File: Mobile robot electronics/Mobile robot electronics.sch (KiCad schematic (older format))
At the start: 17 parts

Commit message: added to schematic:
motor connectors, connections for the motor drivers, started the headers for the ultrasonics
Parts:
- added J? (x4): Conn_01x04_Male, symbol Connector:Conn_01x04_Male
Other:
- note added: "ESP32 MCU\n"
- note added: "Motor Connectors"
- note added: "Motor Drivers\n"

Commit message: added a correct part for ESP32 devkitc v4 wrover
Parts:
- removed U?: ESP32-DEVKITC-32D, MODULE_ESP32-DEVKITC-32D, symbol ESP32-DEVKITC-32D:ESP32-DEVKITC-32D
- added U?: ESP32-DevKitc-V4-WROVER, symbol MCU_ESP:ESP32-DevKitc-V4-WROVER
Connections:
- net labels added: MotorBLA, MotorBLB, MotorBRA, MotorBRB, MotorFLA, MotorFLB, MotorFRA, MotorFRB, Motor_BL_DIR, Motor_BL_PWM, Motor_BR_DIR, Motor_BR_PWM, Motor_FL_DIR, Motor_FL_PWM, Motor_FR_DIR, Motor_FR_PWM
- net labels removed: Motor1A, Motor1B, Motor2A, Motor2B, Motor3A, Motor3B, Motor4A, Motor4B, Motor_1_DIR, Motor_1_PWM, Motor_2_DIR, Motor_2_PWM, Motor_3_DIR, Motor_3_PWM, Motor_4_DIR, Motor_4_PWM
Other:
- note added: "motor BL"
- note added: "motor BR"
- note added: "motor FL"
- note added: "motor FR\n"
- note removed: "motor 1"
- note removed: "motor 2\n"
- note removed: "motor 3"
- note removed: "motor 4"
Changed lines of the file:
@@
 L power:GND #PWR?
 U 1 1 6073A39F
-P 2650 1200
-F 0 "#PWR?" H 2650 950 50  0001 C CNN
-F 1 "GND" V 2655 1072 50  0000 R CNN
-F 2 "" H 2650 1200 50  0001 C CNN
-F 3 "" H 2650 1200 50  0001 C CNN
-	1    2650 1200
+P 2300 2300
+F 0 "#PWR?" H 2300 2050 50  0001 C CNN
+F 1 "GND" V 2305 2172 50  0000 R CNN
+F 2 "" H 2300 2300 50  0001 C CNN
+F 3 "" H 2300 2300 50  0001 C CNN
+	1    2300 2300
 	0    -1   -1   0
 $EndComp
@@
 L power:GND #PWR?
 U 1 1 6073BFC2
-P 2650 1800
-F 0 "#PWR?" H 2650 1550 50  0001 C CNN
-F 1 "GND" V 2655 1672 50  0000 R CNN
-F 2 "" H 2650 1800 50  0001 C CNN
-F 3 "" H 2650 1800 50  0001 C CNN
-	1    2650 1800
+P 2300 2900
+F 0 "#PWR?" H 2300 2650 50  0001 C CNN
+F 1 "GND" V 2305 2772 50  0000 R CNN
+F 2 "" H 2300 2900 50  0001 C CNN
+F 3 "" H 2300 2900 50  0001 C CNN
+	1    2300 2900
 	0    -1   -1   0
 $EndComp
@@
 L power:GND #PWR?
 U 1 1 6073C1A2
-P 1050 2500
-F 0 "#PWR?" H 1050 2250 50  0001 C CNN
-F 1 "GND" V 1055 2372 50  0000 R CNN
-F 2 "" H 1050 2500 50  0001 C CNN
-F 3 "" H 1050 2500 50  0001 C CNN
-	1    1050 2500
+P 1350 1600
+F 0 "#PWR?" H 1350 1350 50  0001 C CNN
+F 1 "GND" V 1355 1472 50  0000 R CNN
+F 2 "" H 1350 1600 50  0001 C CNN
+F 3 "" H 1350 1600 50  0001 C CNN
+	1    1350 1600
 	0    1    1    0
 $EndComp
@@
 L power:+5V #PWR?
 U 1 1 6073C466
-P 1050 3000
-F 0 "#PWR?" H 1050 2850 50  0001 C CNN
-F 1 "+5V" V 1065 3128 50  0000 L CNN
-F 2 "" H 1050 3000 50  0001 C CNN
-F 3 "" H 1050 3000 50  0001 C CNN
-	1    1050 3000
+P 1350 1100
+F 0 "#PWR?" H 1350 950 50  0001 C CNN
+F 1 "+5V" V 1365 1228 50  0000 L CNN
+F 2 "" H 1350 1100 50  0001 C CNN
+F 3 "" H 1350 1100 50  0001 C CNN
+	1    1350 1100
 	0    -1   -1   0
 $EndComp
@@
 	5400 1650 5400 1700
 $Comp
-L ESP32-DEVKITC-32D:ESP32-DEVKITC-32D U?
-U 1 1 60738593
-P 1850 2100
-F 0 "U?" H 1850 3267 50  0000 C CNN
-F 1 "ESP32-DEVKITC-32D" H 1850 3176 50  0000 C CNN
-F 2 "MODULE_ESP32-DEVKITC-32D" H 1850 2100 50  0001 L BNN
-F 3 "" H 1850 2100 50  0001 L BNN
-F 4 "Espressif Systems" H 1850 2100 50  0001 L BNN "MANUFACTURER"
-F 5 "4" H 1850 2100 50  0001 L BNN "PARTREV"
-	1    1850 2100
-	1    0    0    -1
-$EndComp
-$Comp
 L power:+3.3V #PWR?
 U 1 1 60747A00
-P 1050 1200
-F 0 "#PWR?" H 1050 1050 50  0001 C CNN
-F 1 "+3.3V" V 1065 1328 50  0000 L CNN
-F 2 "" H 1050 1200 50  0001 C CNN
-F 3 "" H 1050 1200 50  0001 C CNN
-	1    1050 1200
+P 1350 2900
+F 0 "#PWR?" H 1350 2750 50  0001 C CNN
+F 1 "+3.3V" V 1365 3028 50  0000 L CNN
+F 2 "" H 1350 2900 50  0001 C CNN
+F 3 "" H 1350 2900 50  0001 C CNN
+	1    1350 2900
 	0    -1   -1   0
 $EndComp
@@
 $EndComp
 Text GLabel 5400 1400 2    50   Input ~ 0
-Motor1A
+MotorFLA
 Text GLabel 5400 1500 2    50   Input ~ 0
-Motor1B
+MotorFLB
 Text GLabel 7500 1400 2    50   Input ~ 0
-Motor2A
+MotorFRA
 Text GLabel 7500 1500 2    50   Input ~ 0
-Motor2B
+MotorFRB
 Text GLabel 7500 2600 2    50   Input ~ 0
-Motor4B
+MotorBRB
 Text GLabel 5400 2600 2    50   Input ~ 0
-Motor3B
+MotorBLB
 Text GLabel 5400 2500 2    50   Input ~ 0
-Motor3A
+MotorBLA
 Text GLabel 7500 2500 2    50   Input ~ 0
-Motor4A
+MotorBRA
 $Comp
 L Connector:Conn_01x06_Male J?
@@
 $EndComp
 Text Notes 8800 950  0    50   ~ 0
-motor 1
+motor FL
 Text Notes 10100 950  0    50   ~ 0
-motor 2\n
+motor FR\n
 Text Notes 8850 2250 0    50   ~ 0
-motor 3
+motor BL
 Text Notes 10150 2250 0    50   ~ 0
-motor 4
-Text GLabel 8800 1100 2    50   Input ~ 0
-Motor1A
-Text GLabel 8800 1200 2    50   Input ~ 0
-Motor1B
-Text GLabel 8850 2500 2    50   Input ~ 0
-Motor3B
-Text GLabel 8850 2400 2    50   Input ~ 0
-Motor3A
-Text GLabel 10150 2500 2    50   Input ~ 0
-Motor4B
-Text GLabel 10150 2400 2    50   Input ~ 0
-Motor4A
-Text GLabel 10100 1100 2    50   Input ~ 0
-Motor2A
-Text GLabel 10100 1200 2    50   Input ~ 0
-Motor2B
+motor BR
 $Comp
 L power:GND #PWR?
@@
 $EndComp
 Text GLabel 4500 1500 0    50   Input ~ 0
-Motor_1_PWM
+Motor_FL_PWM
 Text GLabel 4500 1600 0    50   Input ~ 0
-Motor_1_DIR
+Motor_FL_DIR
 Text GLabel 4500 2600 0    50   Input ~ 0
-Motor_3_PWM
+Motor_BL_PWM
 Text GLabel 4500 2700 0    50   Input ~ 0
-Motor_3_DIR
-Text GLabel 6600 2600 0    50   Input ~ 0
-Motor_4_PWM
-Text GLabel 6600 2700 0    50   Input ~ 0
-Motor_4_DIR
+Motor_BL_DIR
 Text GLabel 6600 1500 0    50   Input ~ 0
-Motor_2_PWM
-Text GLabel 6600 1600 0    50   Input ~ 0
-Motor_2_DIR
-Text GLabel 1050 1800 0    50   Input ~ 0
-Motor_1_PWM
-Text GLabel 1050 1900 0    50   Input ~ 0
-Motor_1_DIR
-Text GLabel 1050 2000 0    50   Input ~ 0
-Motor_3_PWM
-Text GLabel 1050 2100 0    50   Input ~ 0
-Motor_3_DIR
-Text GLabel 1050 2200 0    50   Input ~ 0
-Motor_2_PWM
-Text GLabel 1050 2300 0    50   Input ~ 0
-Motor_2_DIR
-Text GLabel 1050 2400 0    50   Input ~ 0
-Motor_4_PWM
-Text GLabel 1050 2700 0    50   Input ~ 0
-Motor_4_DIR
-Text GLabel 1050 1600 0    50   Input ~ 0
+Motor_FR_PWM
+Text GLabel 1350 1900 0    50   Input ~ 0
 Motor_EN
 Wire Notes Line
@@
 Text Notes 8000 550  0    50   ~ 0
 Motor Connectors
-Text GLabel 2650 1300 2    50   Input ~ 0
-Encoder_3_A
-Text GLabel 2650 1400 2    50   Input ~ 0
+Text GLabel 2300 1600 2    50   Input ~ 0
 Encoder_3_B
-Text GLabel 2650 2200 2    50   Input ~ 0
+Text GLabel 2300 2100 2    50   Input ~ 0
 Encoder_1_A
-Text GLabel 2650 2300 2    50   Input ~ 0
+Text GLabel 2300 2200 2    50   Input ~ 0
 Encoder_1_B
-Text GLabel 2650 1900 2    50   Input ~ 0
+Text GLabel 2300 1800 2    50   Input ~ 0
 Encoder_2_A
-Text GLabel 2650 2000 2    50   Input ~ 0
+Text GLabel 2300 1900 2    50   Input ~ 0
 Encoder_2_B
-Text GLabel 2650 2400 2    50   Input ~ 0
+Text GLabel 2300 2700 2    50   Input ~ 0
 Encoder_4_A
-Text GLabel 2650 2500 2    50   Input ~ 0
+Text GLabel 2300 2800 2    50   Input ~ 0
 Encoder_4_B
 $Comp
@@
 	0    -1   -1   0
 $EndComp
+Text GLabel 2300 1500 2    50   Input ~ 0
+Encoder_3_A
+Text GLabel 6600 1600 0    50   Input ~ 0
+Motor_FR_DIR
+Text GLabel 6600 2600 0    50   Input ~ 0
+Motor_BR_PWM
+Text GLabel 6600 2700 0    50   Input ~ 0
+Motor_BR_DIR
+Text GLabel 8800 1100 2    50   Input ~ 0
+MotorFLA
+Text GLabel 8800 1200 2    50   Input ~ 0
+MotorFLB
+Text GLabel 8850 2500 2    50   Input ~ 0
+MotorBLB
+Text GLabel 8850 2400 2    50   Input ~ 0
+MotorBLA
+Text GLabel 10150 2500 2    50   Input ~ 0
+MotorBRB
+Text GLabel 10150 2400 2    50   Input ~ 0
+MotorBRA
+Text GLabel 10100 1200 2    50   Input ~ 0
+MotorFRB
+Text GLabel 10100 1100 2    50   Input ~ 0
+MotorFRA
+Text GLabel 1350 1700 0    50   Input ~ 0
+Motor_FL_PWM
+Text GLabel 1350 1800 0    50   Input ~ 0
+Motor_FL_DIR
+Text GLabel 1350 2200 0    50   Input ~ 0
+Motor_FR_PWM
+Text GLabel 1350 2300 0    50   Input ~ 0
+Motor_FR_DIR
+Text GLabel 1350 2000 0    50   Input ~ 0
+Motor_BL_PWM
+Text GLabel 1350 2100 0    50   Input ~ 0
+Motor_BL_DIR
+Text GLabel 1350 2400 0    50   Input ~ 0
+Motor_BR_PWM
+Text GLabel 1350 2500 0    50   Input ~ 0
+Motor_BR_DIR
+$Comp
+L MCU_ESP:ESP32-DevKitc-V4-WROVER U?
+U 1 1 608569C9
+P 1800 900
+F 0 "U?" H 1825 925 50  0000 C CNN
+F 1 "ESP32-DevKitc-V4-WROVER" H 1825 834 50  0000 C CNN
+F 2 "" H 1800 900 50  0001 C CNN
+F 3 "" H 1800 900 50  0001 C CNN
+	1    1800 900
+	1    0    0    -1
+$EndComp
+$Comp
+L power:GND #PWR?
+U 1 1 6085C50F
+P 1350 1200
+F 0 "#PWR?" H 1350 950 50  0001 C CNN
+F 1 "GND" V 1355 1072 50  0000 R CNN
+F 2 "" H 1350 1200 50  0001 C CNN
+F 3 "" H 1350 1200 50  0001 C CNN
+	1    1350 1200
+	0    1    1    0
+$EndComp
 $EndSCHEMATC

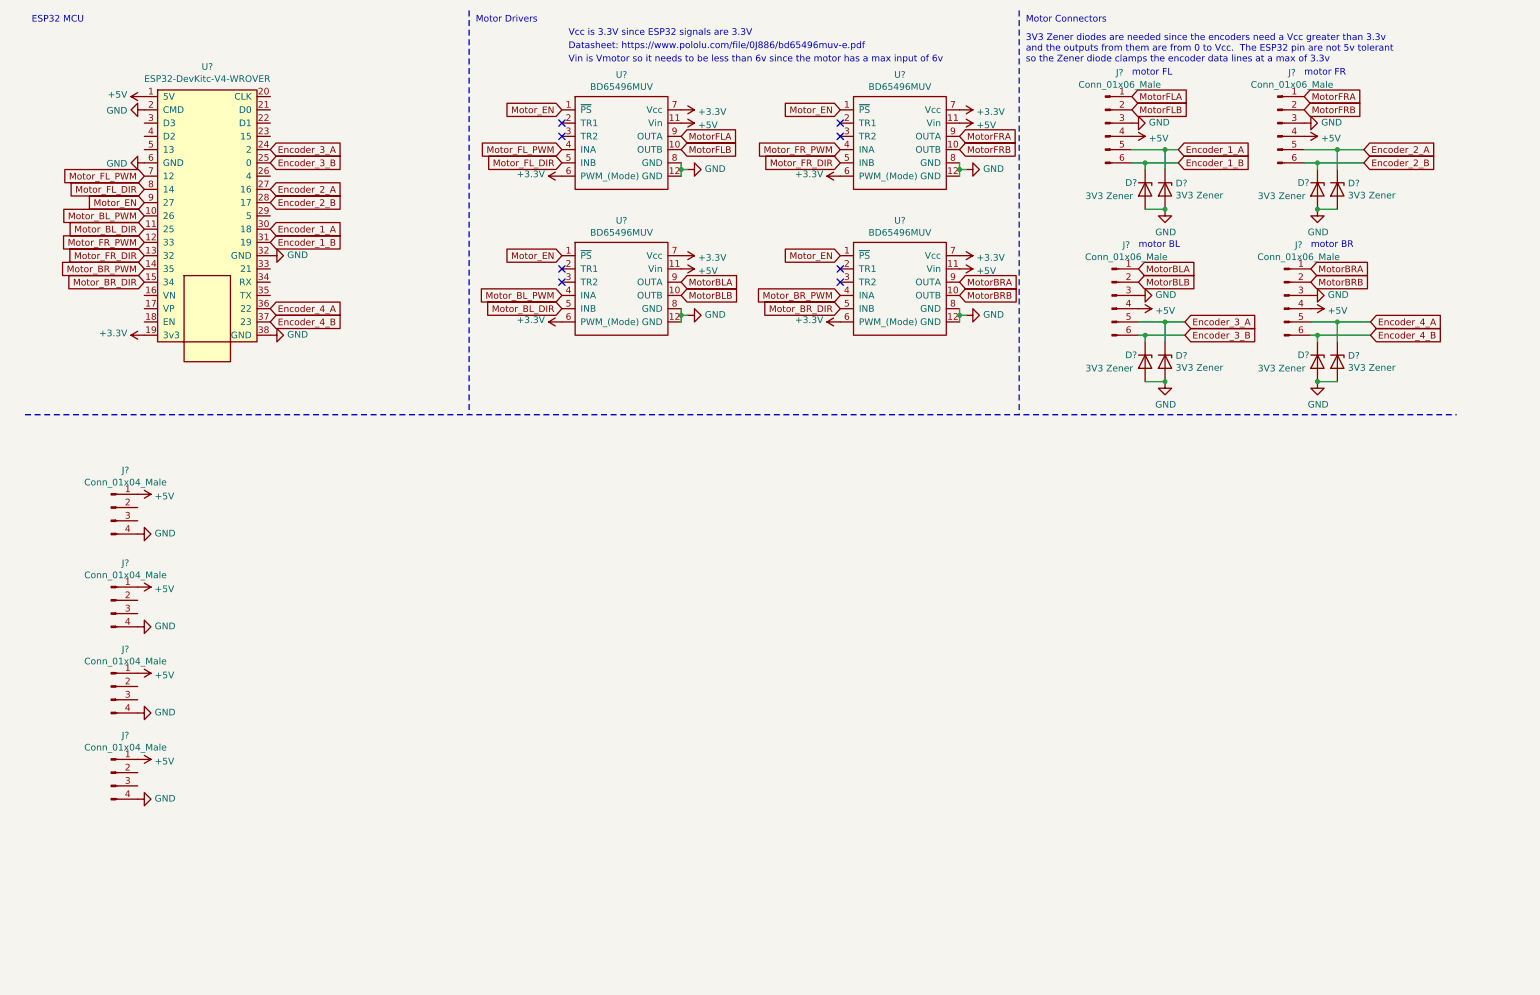
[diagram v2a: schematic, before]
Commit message: Finished the schematic...for now, started PCB
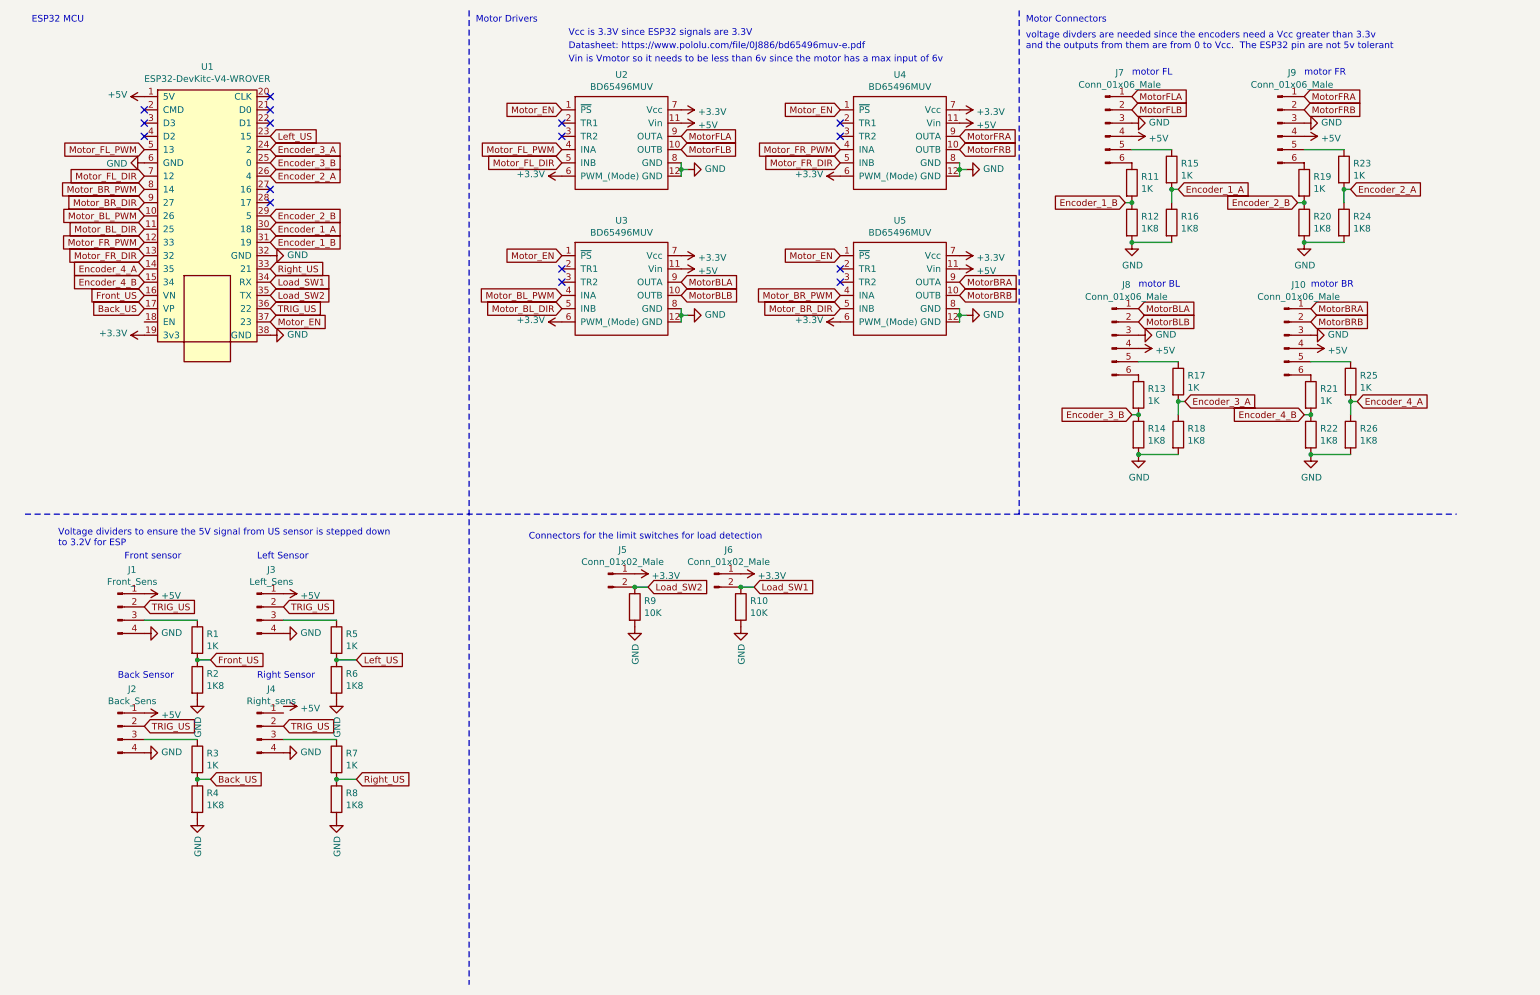
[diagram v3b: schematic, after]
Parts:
- removed D? (x8): 3V3 Zener, symbol Device:D_Zener
- added J5, J6: Conn_01x02_Male, Connector_PinHeader_2.54mm:PinHeader_1x02_P2.54mm_Vertical, symbol Connector:Conn_01x02_Male
- added R1, R11, R13, R15, R17, R19, R21, R23, R25, R3, R5, R7: 1K, Resistor_THT:R_Axial_DIN0207_L6.3mm_D2.5mm_P10.16mm_Horizontal, symbol Device:R
- added R10, R9: 10K, Resistor_THT:R_Axial_DIN0207_L6.3mm_D2.5mm_P10.16mm_Horizontal, symbol Device:R
- added R12, R14, R16, R18, R2, R20, R22, R24, R26, R4, R6, R8: 1K8, Resistor_THT:R_Axial_DIN0207_L6.3mm_D2.5mm_P10.16mm_Horizontal, symbol Device:R
- J1: renamed from J?; value Conn_01x04_Male -> Front_Sens; footprint (none) -> Connector_PinHeader_2.54mm:PinHeader_1x04_P2.54mm_Vertical
- J10, J7, J8, J9: renamed from J?; footprint (none) -> Connector_PinHeader_2.54mm:PinHeader_1x06_P2.54mm_Vertical
- J2: renamed from J?; value Conn_01x04_Male -> Back_Sens; footprint (none) -> Connector_PinHeader_2.54mm:PinHeader_1x04_P2.54mm_Vertical
- J3: renamed from J?; value Conn_01x04_Male -> Left_Sens; footprint (none) -> Connector_PinHeader_2.54mm:PinHeader_1x04_P2.54mm_Vertical
- J4: renamed from J?; value Conn_01x04_Male -> Right_sens; footprint (none) -> Connector_PinHeader_2.54mm:PinHeader_1x04_P2.54mm_Vertical
- U1: renamed from U?; footprint (none) -> ESP32-DEVKITC-32D:ESP32-DevKitC-V4-WROVER
- U2, U3, U4, U5: renamed from U?; footprint (none) -> Motor_driver:BD65496MUV_Carrier
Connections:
- net +3V3: now also J5.1 (Pin_1), J6.1 (Pin_1)
- net +5V: no longer J4.1 (Pin_1)
- net Encoder_1_A: now also R15.2, R16.1; no longer J7.5 (Pin_5)
- net Encoder_1_B: now also R11.2, R12.1; no longer J7.6 (Pin_6)
- net Encoder_2_A: now also U1.26 (4), R23.2, R24.1; no longer J9.5 (Pin_5), U1.27 (16)
- net Encoder_2_B: now also U1.29 (5), R19.2, R20.1; no longer J9.6 (Pin_6), U1.28 (17)
- net Encoder_3_A: now also R17.2, R18.1; no longer J8.5 (Pin_5)
- net Encoder_3_B: now also R13.2, R14.1; no longer J8.6 (Pin_6)
- net Encoder_4_A: now also U1.14 (35), R25.2, R26.1; no longer J10.5 (Pin_5), U1.36 (22)
- net Encoder_4_B: now also U1.15 (34), R21.2, R22.1; no longer J10.6 (Pin_6), U1.37 (23)
- net GND: now also R10.2, R12.2, R14.2, R16.2, R18.2, R2.2, R20.2, R22.2, R24.2, R26.2, R4.2, R6.2, R8.2, R9.2; no longer U1.2 (CMD)
- net Motor_BR_DIR: now also U1.9 (27); no longer U1.15 (34)
- net Motor_BR_PWM: now also U1.8 (14); no longer U1.14 (35)
- net Motor_EN: now also U1.37 (23); no longer U1.9 (27)
- net Motor_FL_DIR: now also U1.7 (12); no longer U1.8 (14)
- net Motor_FL_PWM: now also U1.5 (13); no longer U1.7 (12)
- net TRIG_US: now reaches J1.2 (Pin_2)
- net TRIG_US: now also J2.2 (Pin_2), J3.2 (Pin_2), J4.2 (Pin_2), U1.36 (22)
- net at J1.3 (Pin_3): now also R1.1
- net at J2.3 (Pin_3): now also R3.1
- net at J3.3 (Pin_3): now also R5.1
- net at J4.3 (Pin_3): now also R7.1
- net Front_US: now reaches U1.16 (VN)
- net Front_US: now also R1.2, R2.1
- net Back_US: now reaches U1.17 (VP)
- net Back_US: now also R3.2, R4.1
- net Left_US: now reaches U1.23 (15)
- net Left_US: now also R5.2, R6.1
- net Right_US: now reaches U1.33 (21)
- net Right_US: now also R7.2, R8.1
- net Load_SW1: now reaches U1.34 (RX)
- net Load_SW1: now also J6.2 (Pin_2), R10.1
- net Load_SW2: now reaches U1.35 (TX)
- net Load_SW2: now also J5.2 (Pin_2), R9.1
- new net: J7.5 (Pin_5), R15.1
- new net: J7.6 (Pin_6), R11.1
- new net: J9.5 (Pin_5), R23.1
- new net: J9.6 (Pin_6), R19.1
- new net: J8.5 (Pin_5), R17.1
- new net: J8.6 (Pin_6), R13.1
- new net: J10.5 (Pin_5), R25.1
- new net: J10.6 (Pin_6), R21.1
- no-connect marks 8 -> 16
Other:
- note added: "Back Sensor"
- note added: "Connectors for the limit switches for load detection\n"
- note added: "Front sensor\n"
- note added: "Left Sensor\n"
- note added: "Right Sensor"
- note added: "Voltage dividers to ensure the 5V signal from US sensor is stepped down\nto 3.2V for ESP"
- note added: "voltage divders are needed since the encoders need a Vcc greater than 3.3v\nand the outputs from them are from 0 to Vcc. The ESP32 pin are not 5v tolerant"
- note removed: "3V3 Zener diodes are needed since the encoders need a Vcc greater than 3.3v\nand the outputs from them are from 0 to Vcc. The ESP32 pin are not 5v tolerant\nso the Zener diode clamps the encoder data lines at a max of 3.3v"
- moved on the sheet: J1, J10, J2, J3, J4, J8
